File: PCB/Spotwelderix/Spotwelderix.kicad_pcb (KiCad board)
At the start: 2 copper layers, 128.5 x 64.3 mm, 54 parts, among them IC1 INA213AIDCKR, IC2 IXDD604SIA, IC3 IXDD604SIA, J1 OnOffTast, J4 probe-, P1 CONN_01X09, Q1 IRFB7430, Q10 FQP27P06, Q2 IRFB7430, Q3 IRFB7430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

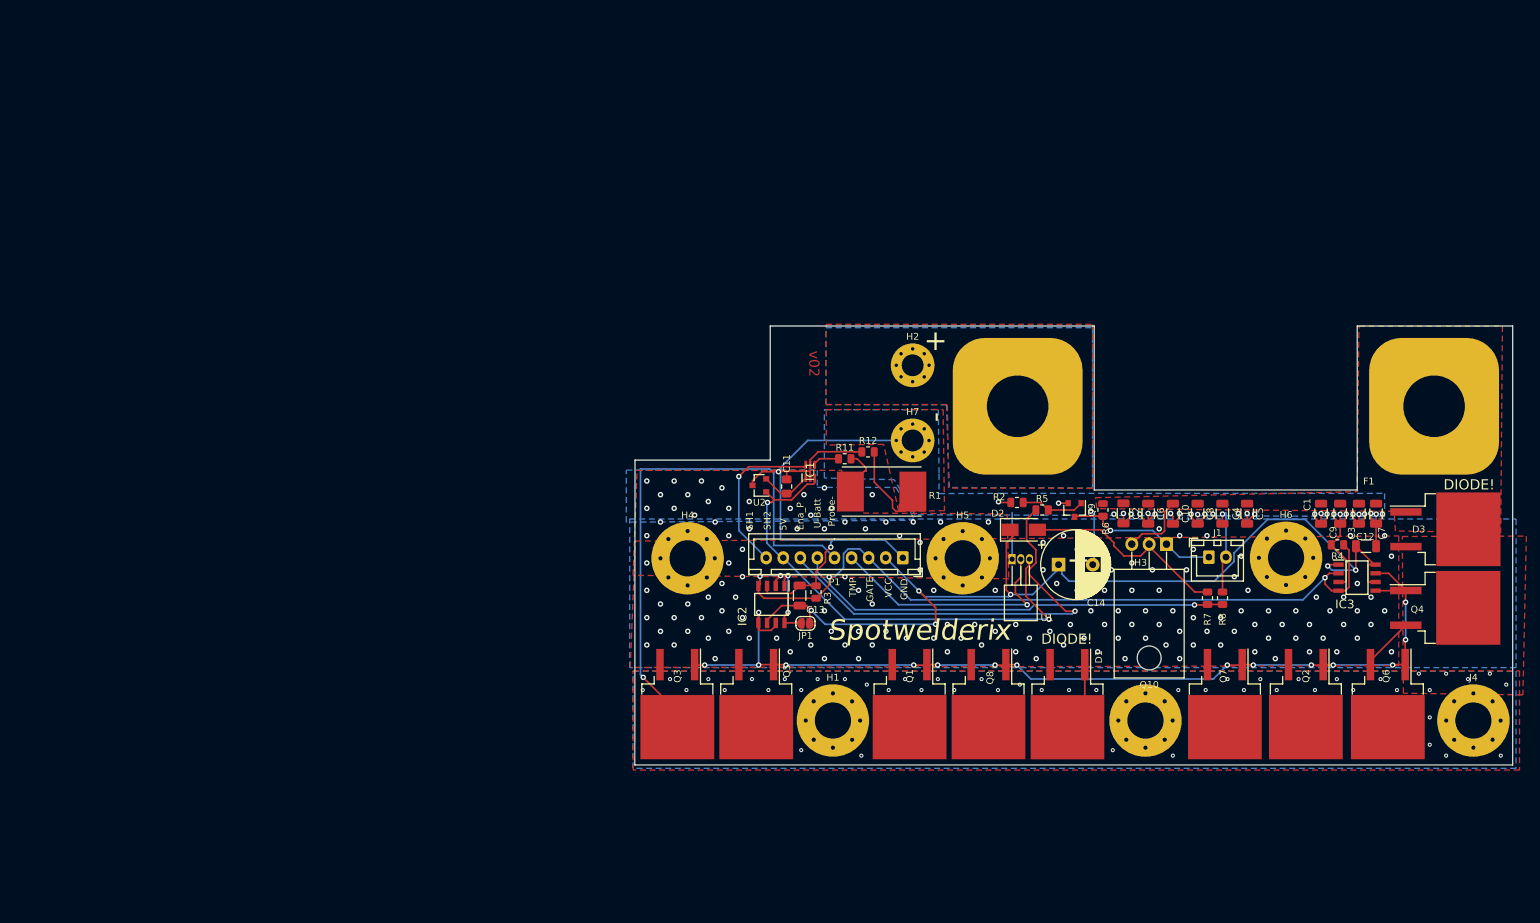
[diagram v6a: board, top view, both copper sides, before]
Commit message: PCB v2 , Power PCB routed
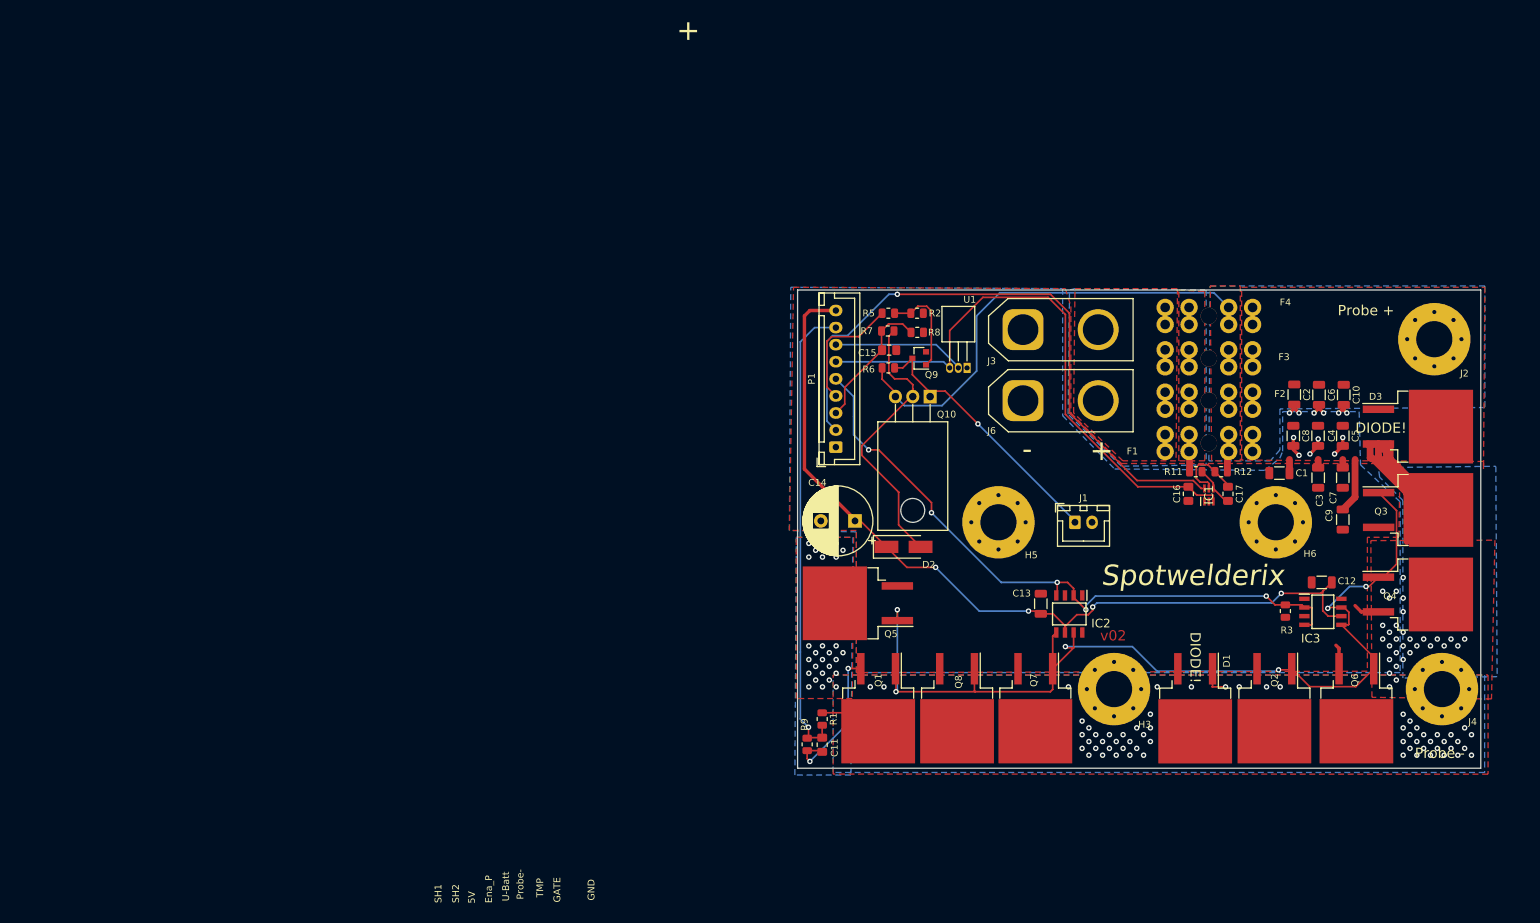
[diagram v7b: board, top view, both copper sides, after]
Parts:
- removed H1, H4: MountingHole_Pad, MountingHole:MountingHole_5.3mm_M5_Pad_Via
- removed H2, H7: MountingHole_Pad, MountingHole:MountingHole_3.2mm_M3_Pad_Via
- removed JP1: Jumper_NO_Small, Jumper:SolderJumper-2_P1.3mm_Open_RoundedPad1.0x1.5mm
- removed R4: 10k, Resistor_SMD:R_0805_2012Metric
- removed U2: REF3020, Package_TO_SOT_SMD:SOT-23
- added C15: 10n, Capacitor_SMD:C_0805_2012Metric_Pad1.18x1.45mm_HandSolder, F.Cu at (113.4, 68.8)
- added C16: 100n, Capacitor_SMD:C_0805_2012Metric_Pad1.18x1.45mm_HandSolder, F.Cu at (157.2, 89.8)
- added C17: 1µ, Capacitor_SMD:C_0805_2012Metric_Pad1.18x1.45mm_HandSolder, F.Cu at (163.0, 89.8)
- added F2: 50A, my_parts:IMAXX_H1810-2x4, F.Cu at (160.2, 76.2)
- added F3: 50A, my_parts:IMAXX_H1810-2x4, F.Cu at (160.2, 70.0)
- added F4: 50A, my_parts:IMAXX_H1810-2x4, F.Cu at (160.2, 63.8)
- added J2: probe+, MountingHole:MountingHole_5.3mm_M5_Pad_Via, F.Cu at (193.2, 67.2)
- added J3: Conn_01x02_Male, my_parts:AMASS_XT60-M_1x02_P7.20mm_Vertical, F.Cu at (133.0, 65.8)
- added J6: Conn_01x02_Male, my_parts:AMASS_XT60-M_1x02_P7.20mm_Vertical, F.Cu at (133.0, 76.2)
- added R9: 2.5k, Resistor_SMD:R_0805_2012Metric, F.Cu at (101.4, 126.5)
- C11: value 100n -> 10n
- D2: footprint Diode_SMD:D_SMA -> Diode_SMD:D_SMA_Handsoldering
- F1: value 300A -> 50A; footprint my_parts:ANL_Fuse -> my_parts:IMAXX_H1810-2x4
- R1: value 100µ -> 15k; footprint Resistor_SMD:R_Shunt_Vishay_WSR2_WSR3 -> Resistor_SMD:R_0805_2012Metric
- R11, R12: value 30k -> 12
- R7: value 33k -> 15k
- R8: value 6.5k -> 2.5k
- moved Q3 112.1 mm to (190.8, 92.2), turned to 0 degrees
- moved R3 68.8 mm to (171.4, 107.0), turned to 270 degrees
- moved R7 61.0 mm to (113.2, 66.0), turned to 180 degrees
- moved R8 59.3 mm to (117.5, 66.2), turned to 0 degrees
- moved IC1 58.5 mm to (160.2, 90.0)
- moved R12 51.8 mm to (162.0, 86.6)
- moved R11 51.4 mm to (158.3, 86.6), turned to 180 degrees
- moved IC2 43.6 mm to (139.8, 107.4)
- moved Q10 40.8 mm to (119.4, 75.6)
- moved C11 38.2 mm to (103.6, 126.6), turned to 270 degrees
- moved R6 37.7 mm to (113.3, 71.4), turned to 0 degrees
- moved R5 36.5 mm to (113.3, 63.4)
- moved C13 35.3 mm to (135.6, 105.9)
- moved R1 34.4 mm to (103.6, 122.8), turned to 270 degrees
- moved F1 33.4 mm to (160.2, 82.4)
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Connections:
- C11 pad 1: Net-(C11-Pad1) -> ProbeADC
- D1 pad 2: FET_GND -> GND
- H5 pad 1: FET_GND -> GND
- H6 pad 1: FET_GND -> GND
- IC1 pad 1: Net-(C11-Pad1) -> GND
- IC1 pad 3: +5V -> +3V3
- IC2 pad 8: Net-(IC2-Pad1) -> Net-(IC2-Pad8)
- IC3 pad 1: VCC -> Net-(IC3-Pad1)
- IC3 pad 8: VCC -> Net-(IC3-Pad8)
- P1 pad 2: VCC -> R_Schunt_Stab
- P1 pad 3: Gate_logic -> V_Batt
- P1 pad 4: Dallas -> EnablePower
- P1 pad 5: Probe- -> Gate_logic
- P1 pad 6: V_Batt -> +3V3
- P1 pad 7: EnablePower -> Dallas
- P1 pad 8: +5V -> ProbeADC
- P1 pad 9: R_Schunt_Stab -> VCC
- Q1 pad 3: FET_GND -> GND
- Q2 pad 3: FET_GND -> GND
- Q3 pad 3: FET_GND -> GND
- Q4 pad 3: FET_GND -> GND
- Q5 pad 3: FET_GND -> GND
- Q6 pad 3: FET_GND -> GND
- Q7 pad 3: FET_GND -> GND
- Q8 pad 3: FET_GND -> GND
- R1 pad 1: FET_GND -> Probe-
- R1 pad 2: GND -> ProbeADC
- R11 pad 2: FET_GND -> +BATT
- R12 pad 2: GND -> VCCQ
- U1 pad 3: +5V -> +3V3
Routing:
- net GND: track 189.1 -> 46.1 mm, vias 33 -> 14
- net +3V3: track 0.00 -> 84.5 mm
- net +5V: track 73.0 -> 0.00 mm, vias 2 -> 0
- net VCCQ: track 10.1 -> 83.0 mm
- net ProbeADC: track 0.00 -> 68.7 mm, vias 0 -> 1
- net R_Schunt_Stab: track 24.4 -> 92.0 mm
- net EnablePower: track 64.1 -> 18.3 mm, vias 1 -> 0
- net V_Batt: track 64.0 -> 20.1 mm, vias 1 -> 0
- net Probe-: track 90.2 -> 59.0 mm, vias 50 -> 117
- net VCC: track 144.7 -> 124.1 mm, vias 6 -> 4
- net Gate_logic: track 113.8 -> 95.9 mm, vias 4 -> 5
- net Dallas: track 36.3 -> 19.4 mm, vias 1 -> 0
- net FET_GND: track 15.5 -> 0.00 mm, vias 156 -> 0
- net Net-(J1-Pad1): track 23.5 -> 38.4 mm
- net Net-(D2-Pad2): track 30.0 -> 41.6 mm
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- added copper zone on B.Cu, net VCCQ
- removed copper zone on B.Cu, net FET_GND
- removed copper zone on F.Cu, net FET_GND
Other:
- board size 128.5 x 64.3 mm -> 100 x 70 mm
- board text added: "3V3"
- board text added: "Gate"
- board text added: "I_sens"
- board text added: "PWR_ON"
- board text added: "Probe +"
- board text added: "Probe -"
- board text added: "Probe-ADC"
- board text added: "V_Batt"

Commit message: clean up
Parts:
- added J5: TestCurr, Connector_PinHeader_2.54mm:PinHeader_1x02_P2.54mm_Vertical, F.Cu at (161.2, 94.0)
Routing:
- net Net-(C17-Pad1): track 10.8 -> 22.5 mm
- net Net-(C17-Pad2): track 6.04 -> 9.91 mm
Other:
- board text removed: "5V"
- board text removed: "Ena_P"
- board text removed: "GATE"
- board text removed: "Probe-"
- board text removed: "SH1"
- board text removed: "SH2"
- board text removed: "U-Batt"
